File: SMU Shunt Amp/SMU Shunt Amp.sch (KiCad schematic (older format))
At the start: 32 parts, among them J1 30VDC, J2 Input, J3 Output, U1 OPA189IDBVx, U2 THS3092D

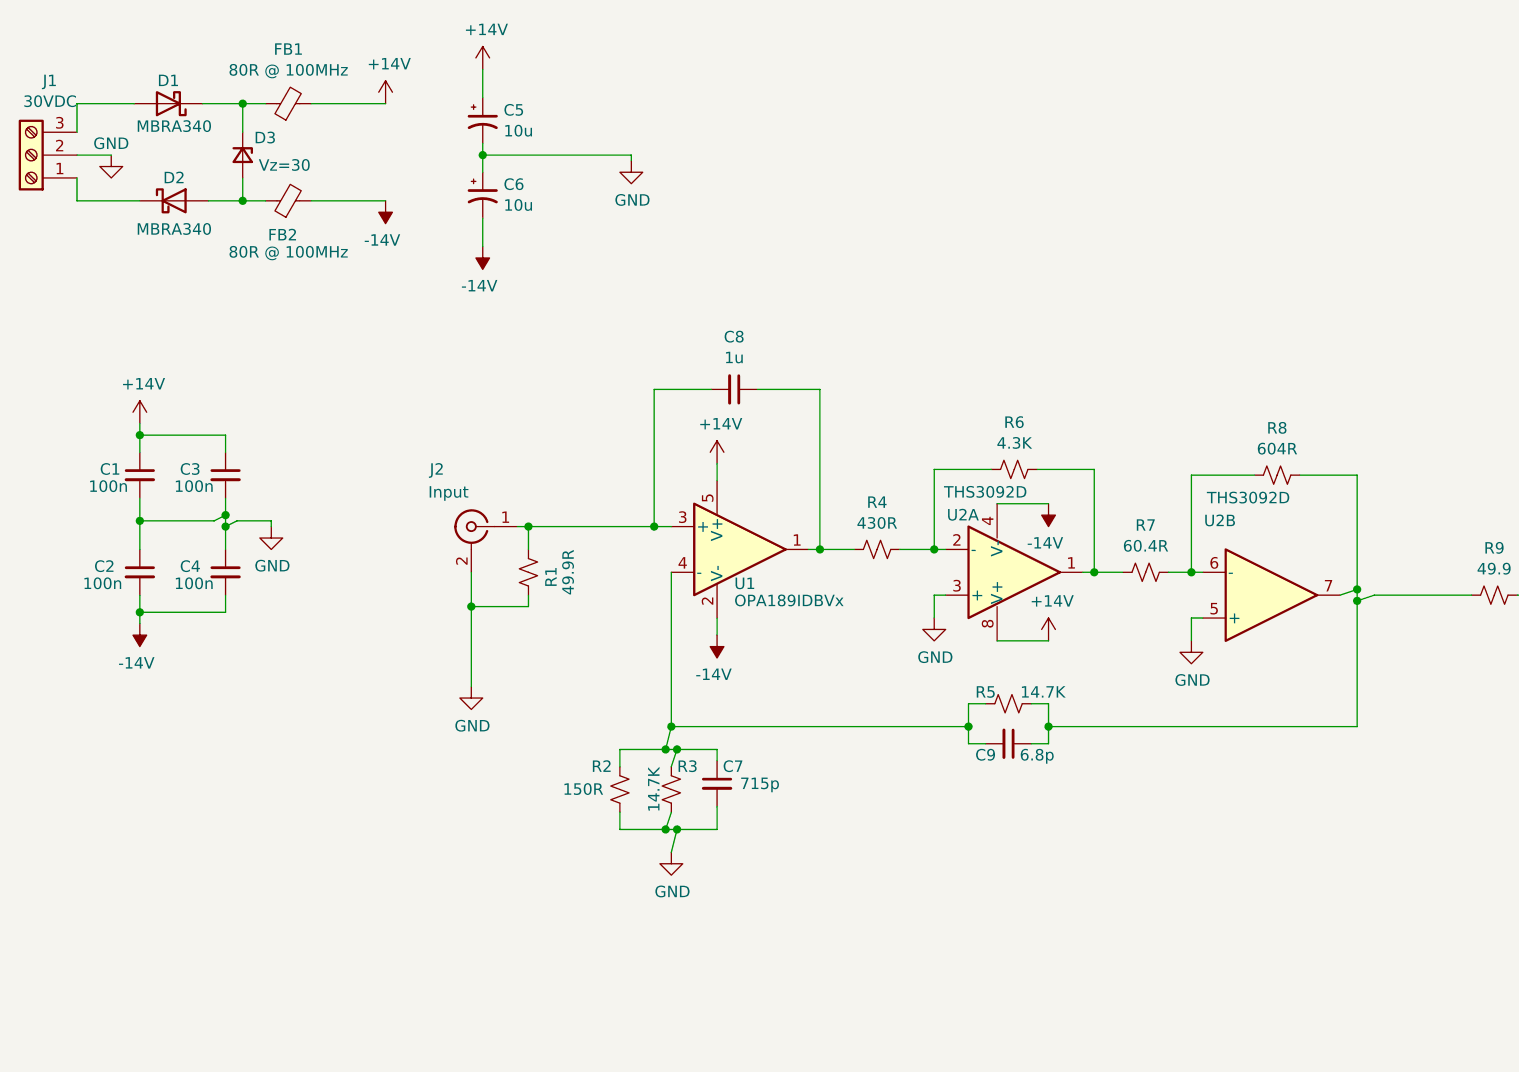
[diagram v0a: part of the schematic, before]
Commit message: Remove fb caps after more sims. Increase fb resistors in hs loop.
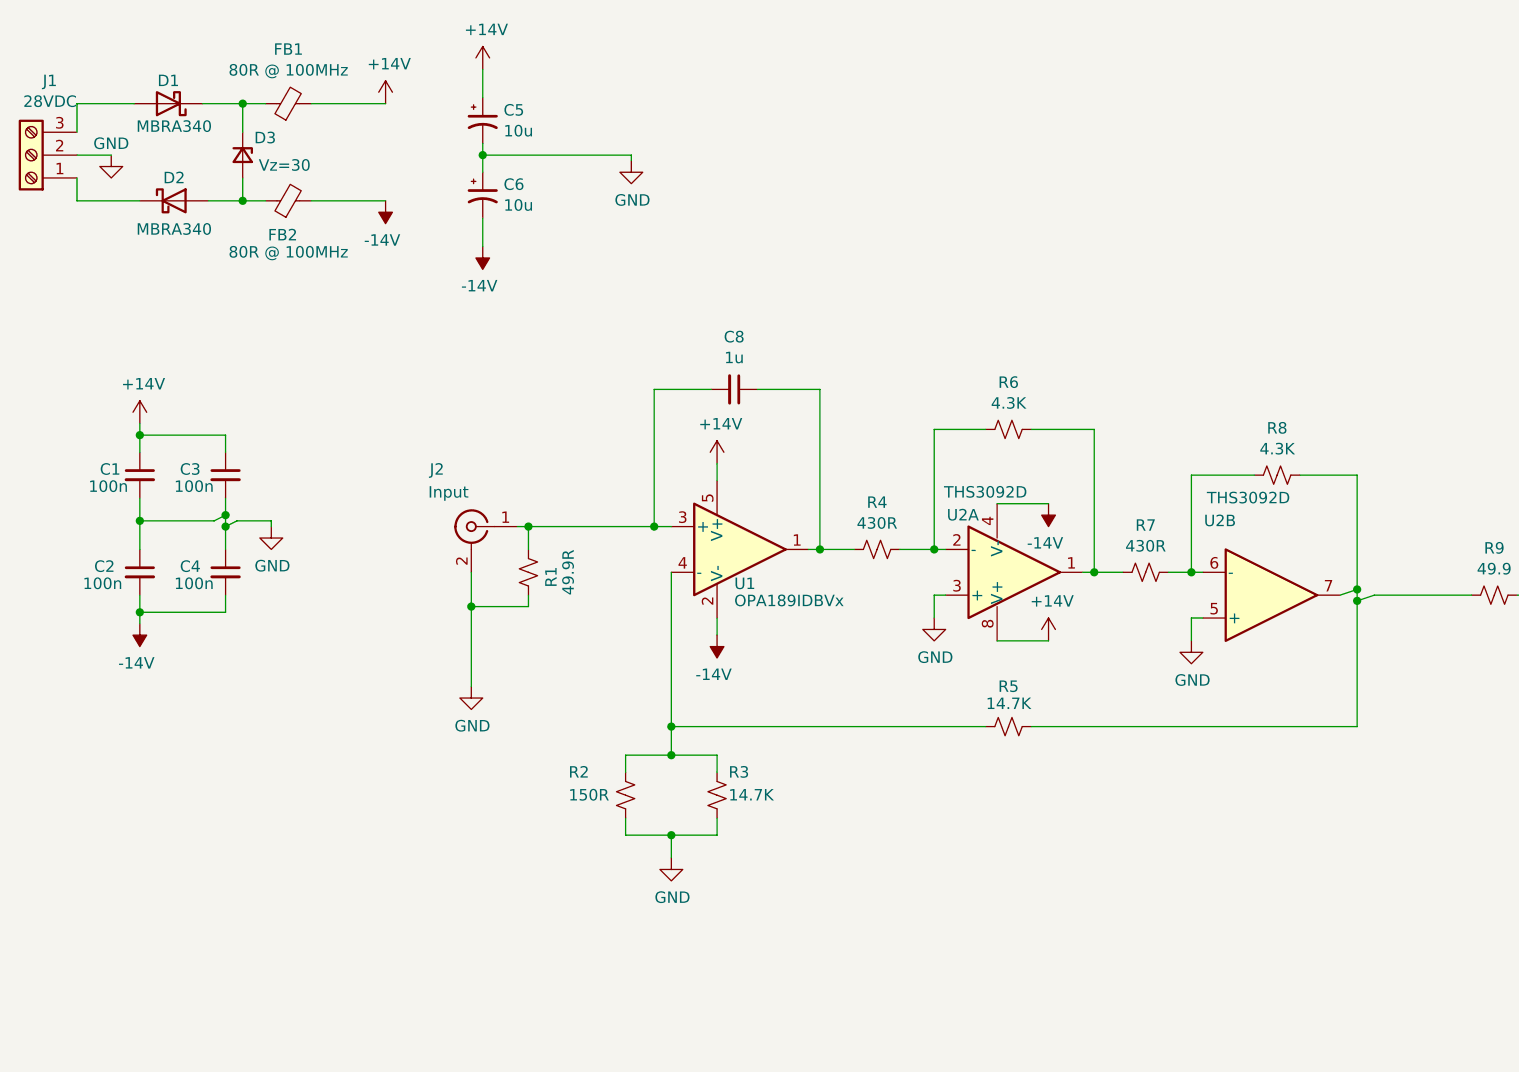
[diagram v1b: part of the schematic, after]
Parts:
- removed C7: 715p, Capacitor_SMD:C_0805_2012Metric_Pad1.18x1.45mm_HandSolder, symbol Device:C_Small
- removed C9: 6.8p, Capacitor_SMD:C_0805_2012Metric_Pad1.18x1.45mm_HandSolder, symbol Device:C_Small
- J1: value 30VDC -> 28VDC
- R7: value 60.4R -> 430R
- R8: value 604R -> 4.3K
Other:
- moved on the sheet: R2, R3, R5, R6
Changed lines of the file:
@@
 P 1325 1800
 F 0 "J1" H 1243 1475 50  0000 C CNN
-F 1 "30VDC" H 1243 1566 50  0000 C CNN
+F 1 "28VDC" H 1243 1566 50  0000 C CNN
 F 2 "TerminalBlock_Phoenix:TerminalBlock_Phoenix_PT-1,5-3-5.0-H_1x03_P5.00mm_Horizontal" H 1325 1800 50  0001 C CNN
 F 3 "~" H 1325 1800 50  0001 C CNN
@@
 $EndComp
 $Comp
-L Device:R_Small_US R6
-U 1 1 609DAC9E
-P 5625 3175
-F 0 "R6" V 5420 3175 50  0000 C CNN
-F 1 "4.3K" V 5511 3175 50  0000 C CNN
-F 2 "Resistor_SMD:R_0805_2012Metric_Pad1.20x1.40mm_HandSolder" H 5625 3175 50  0001 C CNN
-F 3 "~" H 5625 3175 50  0001 C CNN
-	1    5625 3175
-	0    1    1    0
-$EndComp
-$Comp
 L Device:R_Small_US R8
 U 1 1 609DC1E0
 P 6775 3200
 F 0 "R8" V 6570 3200 50  0000 C CNN
-F 1 "604R" V 6661 3200 50  0000 C CNN
+F 1 "4.3K" V 6661 3200 50  0000 C CNN
 F 2 "Resistor_SMD:R_0805_2012Metric_Pad1.20x1.40mm_HandSolder" H 6775 3200 50  0001 C CNN
 F 3 "~" H 6775 3200 50  0001 C CNN
@@
 L Device:R_Small_US R5
 U 1 1 609DD577
-P 5600 4200
-F 0 "R5" V 5550 4100 50  0000 C CNN
-F 1 "14.7K" V 5550 4350 50  0000 C CNN
-F 2 "Resistor_SMD:R_0805_2012Metric_Pad1.20x1.40mm_HandSolder" H 5600 4200 50  0001 C CNN
-F 3 "~" H 5600 4200 50  0001 C CNN
-	1    5600 4200
+P 5600 4300
+F 0 "R5" V 5425 4300 50  0000 C CNN
+F 1 "14.7K" V 5500 4300 50  0000 C CNN
+F 2 "Resistor_SMD:R_0805_2012Metric_Pad1.20x1.40mm_HandSolder" H 5600 4300 50  0001 C CNN
+F 3 "~" H 5600 4300 50  0001 C CNN
+	1    5600 4300
 	0    1    1    0
 $EndComp
@@
 L Device:R_Small_US R2
 U 1 1 609DE88C
-P 3900 4575
-F 0 "R2" H 3775 4675 50  0000 L CNN
-F 1 "150R" H 3650 4575 50  0000 L CNN
-F 2 "Resistor_SMD:R_0805_2012Metric_Pad1.20x1.40mm_HandSolder" H 3900 4575 50  0001 C CNN
-F 3 "~" H 3900 4575 50  0001 C CNN
-	1    3900 4575
+P 3925 4600
+F 0 "R2" H 3675 4700 50  0000 L CNN
+F 1 "150R" H 3675 4600 50  0000 L CNN
+F 2 "Resistor_SMD:R_0805_2012Metric_Pad1.20x1.40mm_HandSolder" H 3925 4600 50  0001 C CNN
+F 3 "~" H 3925 4600 50  0001 C CNN
+	1    3925 4600
 	1    0    0    -1
 $EndComp
@@
 L Device:R_Small_US R3
 U 1 1 609DFC1E
-P 4125 4575
-F 0 "R3" H 4150 4675 50  0000 L CNN
-F 1 "14.7K" V 4050 4475 50  0000 L CNN
-F 2 "Resistor_SMD:R_0805_2012Metric_Pad1.20x1.40mm_HandSolder" H 4125 4575 50  0001 C CNN
-F 3 "~" H 4125 4575 50  0001 C CNN
-	1    4125 4575
+P 4325 4600
+F 0 "R3" H 4375 4700 50  0000 L CNN
+F 1 "14.7K" H 4375 4600 50  0000 L CNN
+F 2 "Resistor_SMD:R_0805_2012Metric_Pad1.20x1.40mm_HandSolder" H 4325 4600 50  0001 C CNN
+F 3 "~" H 4325 4600 50  0001 C CNN
+	1    4325 4600
 	1    0    0    -1
 $EndComp
@@
 P 6200 3625
 F 0 "R7" V 5995 3625 50  0000 C CNN
-F 1 "60.4R" V 6086 3625 50  0000 C CNN
+F 1 "430R" V 6086 3625 50  0000 C CNN
 F 2 "Resistor_SMD:R_0805_2012Metric_Pad1.20x1.40mm_HandSolder" H 6200 3625 50  0001 C CNN
 F 3 "~" H 6200 3625 50  0001 C CNN
@@
 Wire Wire Line
 	6300 3625 6400 3625
-Wire Wire Line
-	5275 3525 5275 3175
-Wire Wire Line
-	5275 3175 5525 3175
 Connection ~ 5275 3525
 Wire Wire Line
 	5275 3525 5325 3525
-Wire Wire Line
-	5725 3175 5975 3175
-Wire Wire Line
-	5975 3175 5975 3625
 Wire Wire Line
 	6400 3625 6400 3200
@@
 	6875 3200 7125 3200
 Wire Wire Line
-	3900 4675 3900 4750
-Wire Wire Line
-	3900 4400 3900 4475
+	3925 4700 3925 4775
+Wire Wire Line
+	3925 4425 3925 4500
 Wire Wire Line
 	4725 3525 4775 3525
@@
 L power:GND #PWR011
 U 1 1 60A0E692
-P 4125 4850
-F 0 "#PWR011" H 4125 4600 50  0001 C CNN
-F 1 "GND" H 4130 4677 50  0000 C CNN
-F 2 "" H 4125 4850 50  0001 C CNN
-F 3 "" H 4125 4850 50  0001 C CNN
-	1    4125 4850
-	1    0    0    -1
-$EndComp
-Wire Wire Line
-	5700 4200 5775 4200
-$Comp
-L Device:C_Small C9
-U 1 1 60A2301A
-P 5600 4375
-F 0 "C9" V 5650 4275 50  0000 C CNN
-F 1 "6.8p" V 5650 4500 50  0000 C CNN
-F 2 "Capacitor_SMD:C_0805_2012Metric_Pad1.18x1.45mm_HandSolder" H 5600 4375 50  0001 C CNN
-F 3 "~" H 5600 4375 50  0001 C CNN
-	1    5600 4375
-	0    1    1    0
-$EndComp
-$Comp
-L Device:C_Small C7
-U 1 1 60A2415B
-P 4325 4550
-F 0 "C7" H 4350 4625 50  0000 L CNN
-F 1 "715p" H 4425 4550 50  0000 L CNN
-F 2 "Capacitor_SMD:C_0805_2012Metric_Pad1.18x1.45mm_HandSolder" H 4325 4550 50  0001 C CNN
-F 3 "~" H 4325 4550 50  0001 C CNN
-	1    4325 4550
-	1    0    0    -1
-$EndComp
-Wire Wire Line
-	4325 4400 4325 4450
-Wire Wire Line
-	4325 4750 4325 4650
-Wire Wire Line
-	4125 4850 4150 4750
-Connection ~ 4150 4750
-Wire Wire Line
-	4150 4750 4325 4750
-Wire Wire Line
-	3900 4400 4100 4400
-Wire Wire Line
-	4125 4300 4100 4400
-Connection ~ 4100 4400
-Wire Wire Line
-	5500 4375 5425 4375
-Wire Wire Line
-	5425 4375 5425 4300
-Wire Wire Line
-	5425 4200 5500 4200
-Wire Wire Line
-	5700 4375 5775 4375
-Wire Wire Line
-	5775 4375 5775 4300
+P 4125 4875
+F 0 "#PWR011" H 4125 4625 50  0001 C CNN
+F 1 "GND" H 4130 4702 50  0000 C CNN
+F 2 "" H 4125 4875 50  0001 C CNN
+F 3 "" H 4125 4875 50  0001 C CNN
+	1    4125 4875
+	1    0    0    -1
+$EndComp
+Wire Wire Line
+	4125 4875 4125 4775
 Connection ~ 5975 3625
 Wire Wire Line
@@
 	6400 3825 6450 3825
 Wire Wire Line
-	4125 4300 5425 4300
-Connection ~ 4125 4300
-Connection ~ 5425 4300
-Wire Wire Line
 	4125 3625 4125 4300
-Wire Wire Line
-	5425 4200 5425 4300
-Wire Wire Line
-	7125 4300 5775 4300
-Connection ~ 5775 4300
-Wire Wire Line
-	5775 4300 5775 4200
 $Comp
 L MAGI_Symbols:-14V #PWR015
@@
 Wire Wire Line
 	2175 3375 2175 3425
-Wire Wire Line
-	4100 4400 4150 4400
-Wire Wire Line
-	3900 4750 4100 4750
-Wire Wire Line
-	4125 4475 4150 4400
-Connection ~ 4150 4400
-Wire Wire Line
-	4150 4400 4325 4400
-Wire Wire Line
-	4125 4675 4100 4750
-Connection ~ 4100 4750
-Wire Wire Line
-	4100 4750 4150 4750
 $Comp
 L Device:D_Zener_Small D3
@@
 	0    -1   -1   0
 $EndComp
+Wire Wire Line
+	4125 4300 5500 4300
+Wire Wire Line
+	5700 4300 7125 4300
+Wire Wire Line
+	3925 4775 4125 4775
+Wire Wire Line
+	4325 4500 4325 4425
+Wire Wire Line
+	3925 4425 4125 4425
+Wire Wire Line
+	4125 4775 4325 4775
+Wire Wire Line
+	4325 4775 4325 4700
+Connection ~ 4125 4775
+Wire Wire Line
+	4125 4425 4125 4300
+Connection ~ 4125 4425
+Wire Wire Line
+	4125 4425 4325 4425
+Connection ~ 4125 4300
+Wire Wire Line
+	5975 3000 5975 3625
+Wire Wire Line
+	5275 3525 5275 3000
+Wire Wire Line
+	5275 3000 5500 3000
+Wire Wire Line
+	5700 3000 5975 3000
+$Comp
+L Device:R_Small_US R6
+U 1 1 609DAC9E
+P 5600 3000
+F 0 "R6" V 5395 3000 50  0000 C CNN
+F 1 "4.3K" V 5486 3000 50  0000 C CNN
+F 2 "Resistor_SMD:R_0805_2012Metric_Pad1.20x1.40mm_HandSolder" H 5600 3000 50  0001 C CNN
+F 3 "~" H 5600 3000 50  0001 C CNN
+	1    5600 3000
+	0    1    1    0
+$EndComp
 $EndSCHEMATC

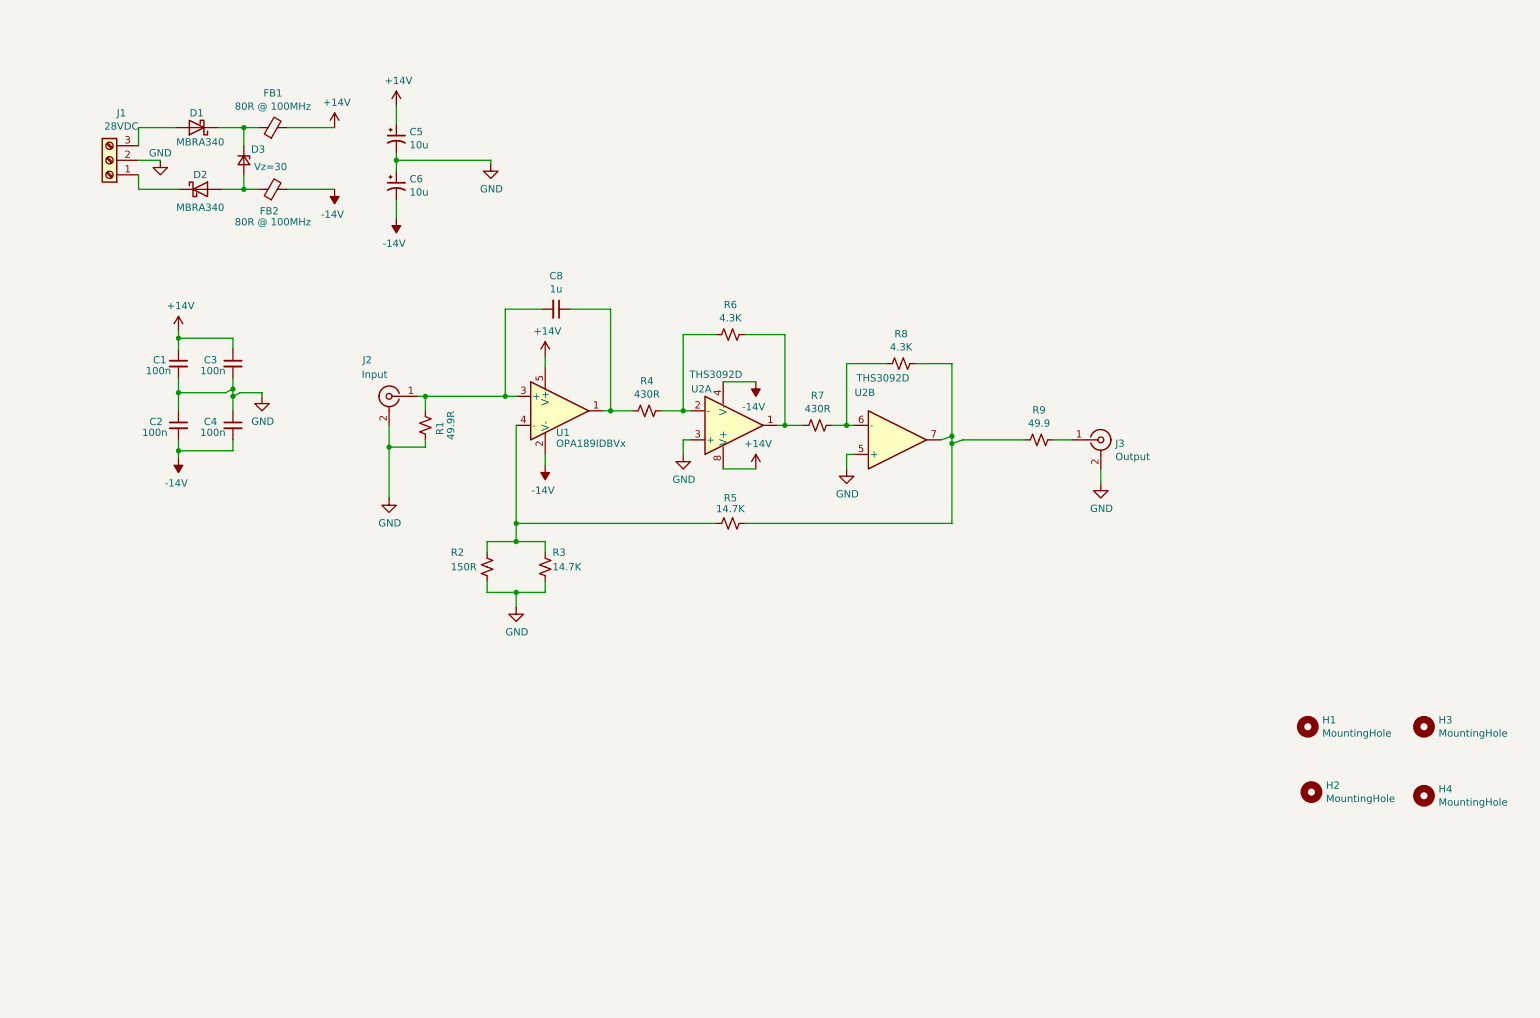
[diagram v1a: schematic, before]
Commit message: Move OPA189 output to THS3092 + for stability
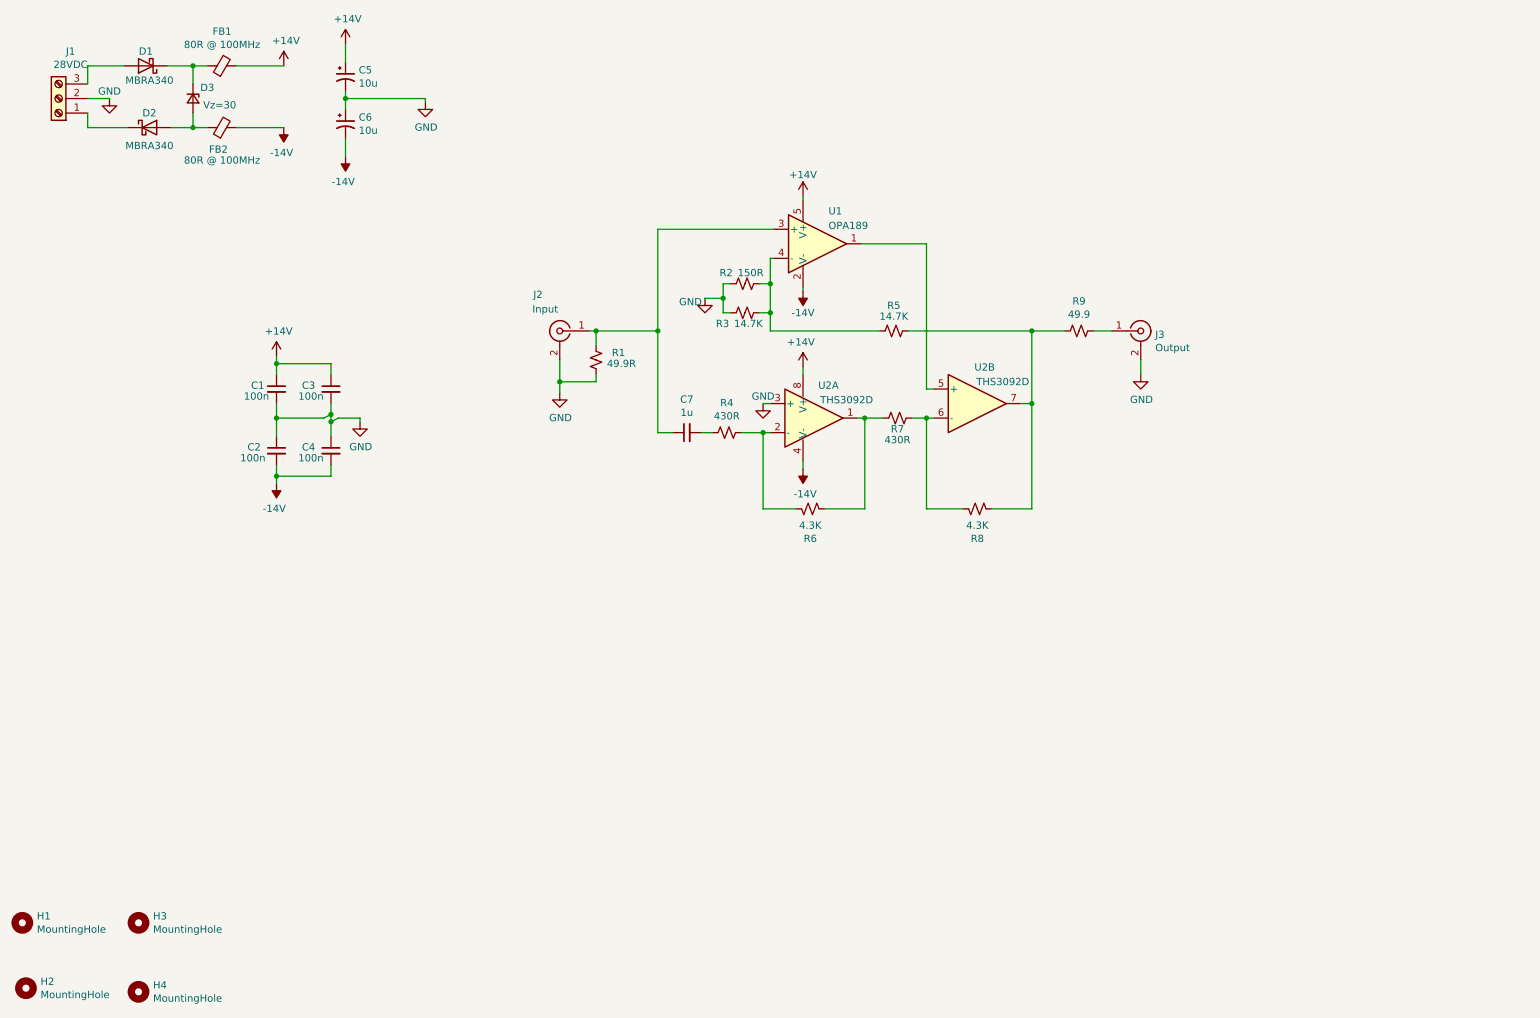
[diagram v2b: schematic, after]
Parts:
- removed C8: 1u, Capacitor_SMD:C_0805_2012Metric_Pad1.18x1.45mm_HandSolder, symbol Device:C_Small
- added C7: 1u, Capacitor_SMD:C_0805_2012Metric_Pad1.18x1.45mm_HandSolder, symbol Device:C_Small
- U1: value OPA189IDBVx -> OPA189
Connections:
- net GND: no longer U2.5 (+)
- net at U1.1: now also U2.5 (+); no longer R4.2
- net at J2.1 (In), R1.2, U1.3 (+): now also C7.1
- new net: C7.2, R4.2
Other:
- moved on the sheet: C1, C2, C3, C4, C5, C6, D1, D2, D3, FB1, FB2, H1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
